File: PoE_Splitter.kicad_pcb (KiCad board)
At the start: 2 copper layers, 104 x 62 mm, 120 parts, among them J1 R-RJ45R10P-B000, J2 R-RJ45R10P-B000, J3 AMASS_XT30PW-M, J4 AMASS_XT30PW-M, J5 AMASS_XT30PW-M, Q1 BSS127S, U1 VCF4812EBO-120WR3-N, U2 TPS2372, U3 MPQ8875A, U4 PD70224, U5 USBLC6-2P6

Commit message: minor cap footprint and value changes
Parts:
- C34, C40: value 2.2uF -> 1uF
- C35, C53: value 2.2uF -> 100nF
- C48, C49: footprint Capacitor_SMD:C_1808_4520Metric -> Capacitor_SMD:C_1812_4532Metric
- moved C48 0.55 mm to (187.8, 104.7)
- moved C49 0.55 mm to (176.1, 104.7)
- moved C28 0.10 mm to (164.2, 107.5)
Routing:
- net AUX_OUT+: vias 5 -> 10

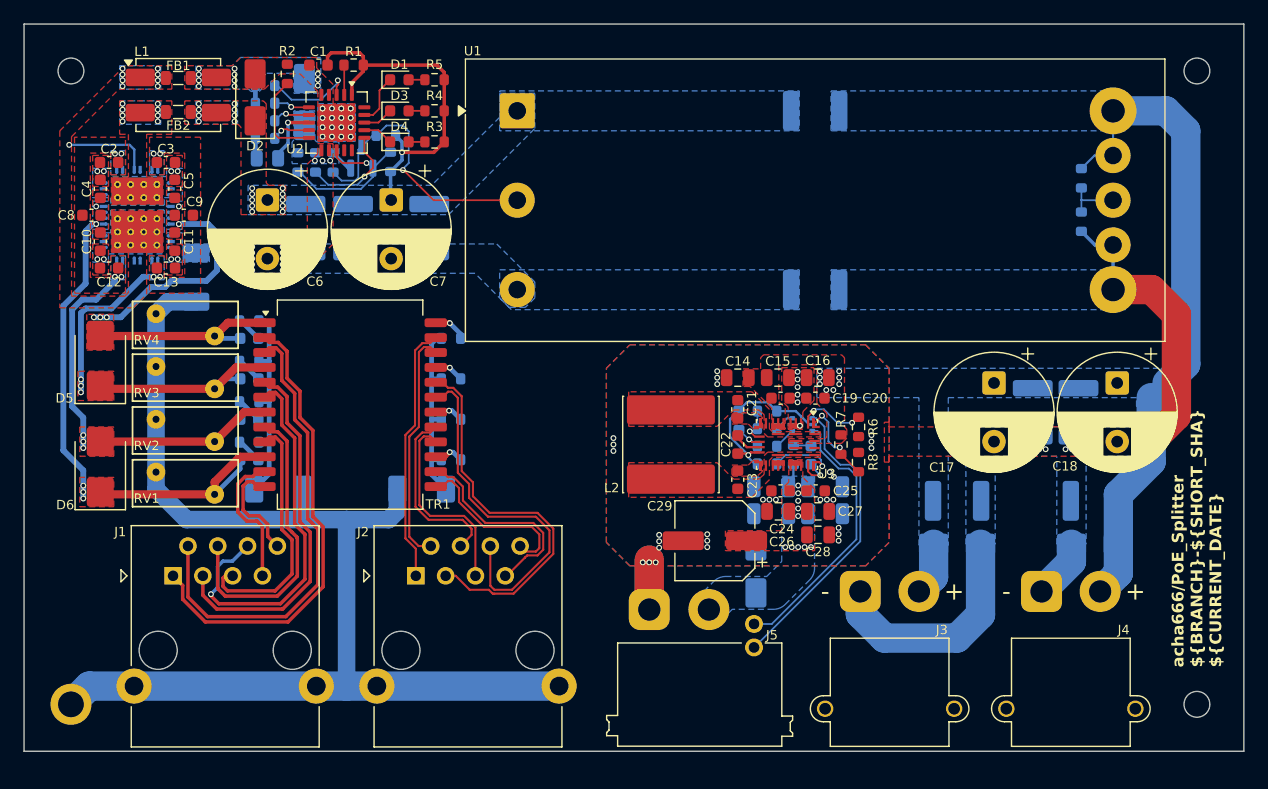
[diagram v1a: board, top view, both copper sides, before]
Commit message: fix: pd70224 input connection
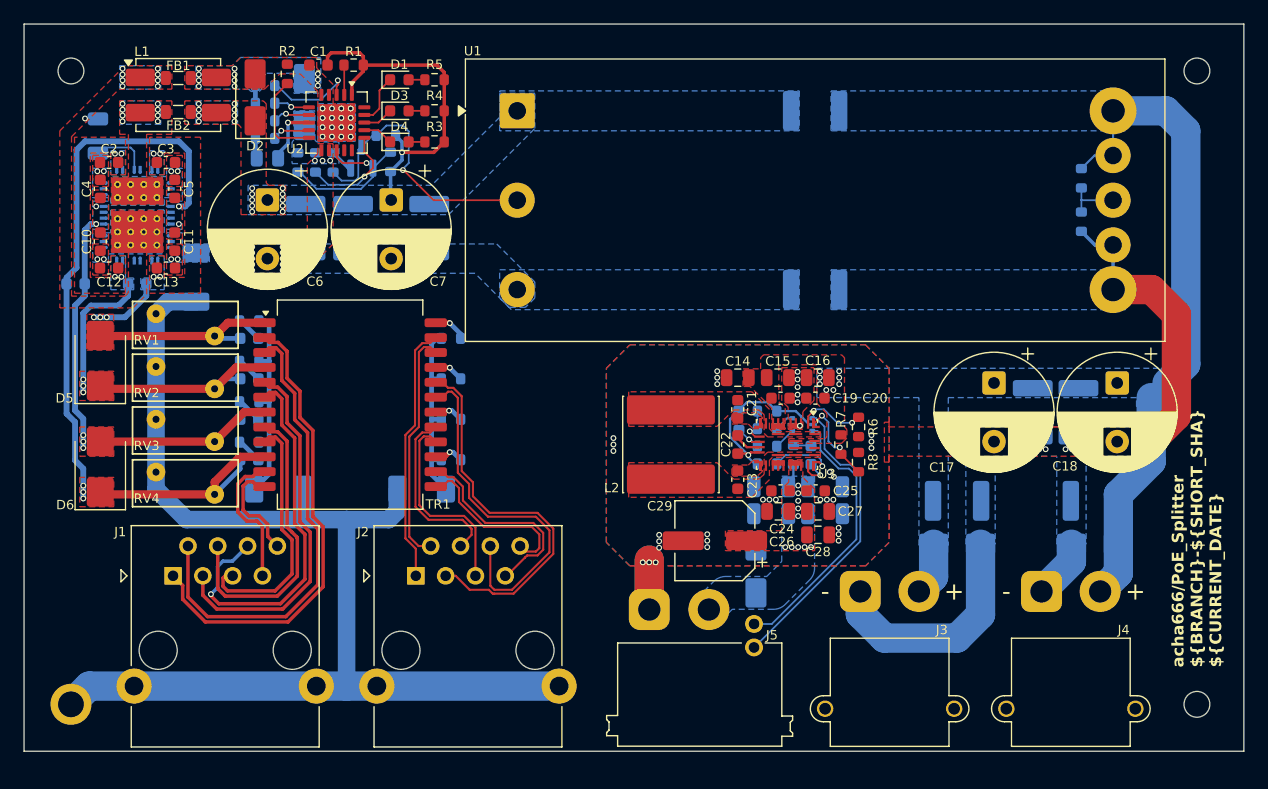
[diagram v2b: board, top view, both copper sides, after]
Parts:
- added R35: 0Ω, Resistor_SMD:R_1206_3216Metric, B.Cu at (102.8, 73.5)
- C8, C9: moved to B.Cu
- moved C9 7.07 mm to (106.2, 86.2), turned to 0 degrees
- moved C8 6.00 mm to (100.9, 86.2), turned to 180 degrees
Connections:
- C10 pad 1: /RJ45 Ports/PS+ -> /RJ45 Ports/PS-
- C11 pad 1: /RJ45 Ports/PD- -> /RJ45 Ports/PS+
- C12 pad 1: /RJ45 Ports/PS- -> /RJ45 Ports/PD+
- C13 pad 1: /RJ45 Ports/PD+ -> /RJ45 Ports/PD-
- C2 pad 2: /RJ45 Ports/PS- -> /RJ45 Ports/PD+
- C3 pad 2: /RJ45 Ports/PD+ -> /RJ45 Ports/PD-
- C4 pad 2: /RJ45 Ports/PS+ -> /RJ45 Ports/PS-
- C5 pad 2: /RJ45 Ports/PD- -> /RJ45 Ports/PS+
- U4 pad 11: /RJ45 Ports/PD+ -> /RJ45 Ports/PD-
- U4 pad 12: /RJ45 Ports/PD+ -> /RJ45 Ports/PD-
- U4 pad 15: /RJ45 Ports/PS- -> /RJ45 Ports/PD+
- U4 pad 16: /RJ45 Ports/PS- -> /RJ45 Ports/PD+
- U4 pad 20: /RJ45 Ports/PS+ -> /RJ45 Ports/PS-
- U4 pad 21: /RJ45 Ports/PS+ -> /RJ45 Ports/PS-
- U4 pad 22: /RJ45 Ports/PS+ -> /RJ45 Ports/PS-
- U4 pad 23: /RJ45 Ports/PS+ -> /RJ45 Ports/PS-
- U4 pad 27: /RJ45 Ports/PS- -> /RJ45 Ports/PD+
- U4 pad 28: /RJ45 Ports/PS- -> /RJ45 Ports/PD+
- U4 pad 29: VRECT- -> Net-(U4-WA_EN)
- U4 pad 31: /RJ45 Ports/PD+ -> /RJ45 Ports/PD-
- U4 pad 32: /RJ45 Ports/PD+ -> /RJ45 Ports/PD-
- U4 pad 4: /RJ45 Ports/PD- -> /RJ45 Ports/PS+
- U4 pad 5: /RJ45 Ports/PD- -> /RJ45 Ports/PS+
- U4 pad 6: /RJ45 Ports/PD- -> /RJ45 Ports/PS+
- U4 pad 7: /RJ45 Ports/PD- -> /RJ45 Ports/PS+
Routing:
- net /RJ45 Ports/PS+: track 45.0 -> 65.9 mm
- net /RJ45 Ports/PD-: track 35.3 -> 22.7 mm, vias 5 -> 7
- net VRECT-: track 7.39 -> 1.12 mm
- net Net-(U4-WA_EN): track 0.00 -> 4.37 mm
- net /RJ45 Ports/PS-: track 35.2 -> 38.4 mm, vias 7 -> 5
- net /RJ45 Ports/PD+: track 31.3 -> 29.2 mm

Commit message: move connectors update 3d models
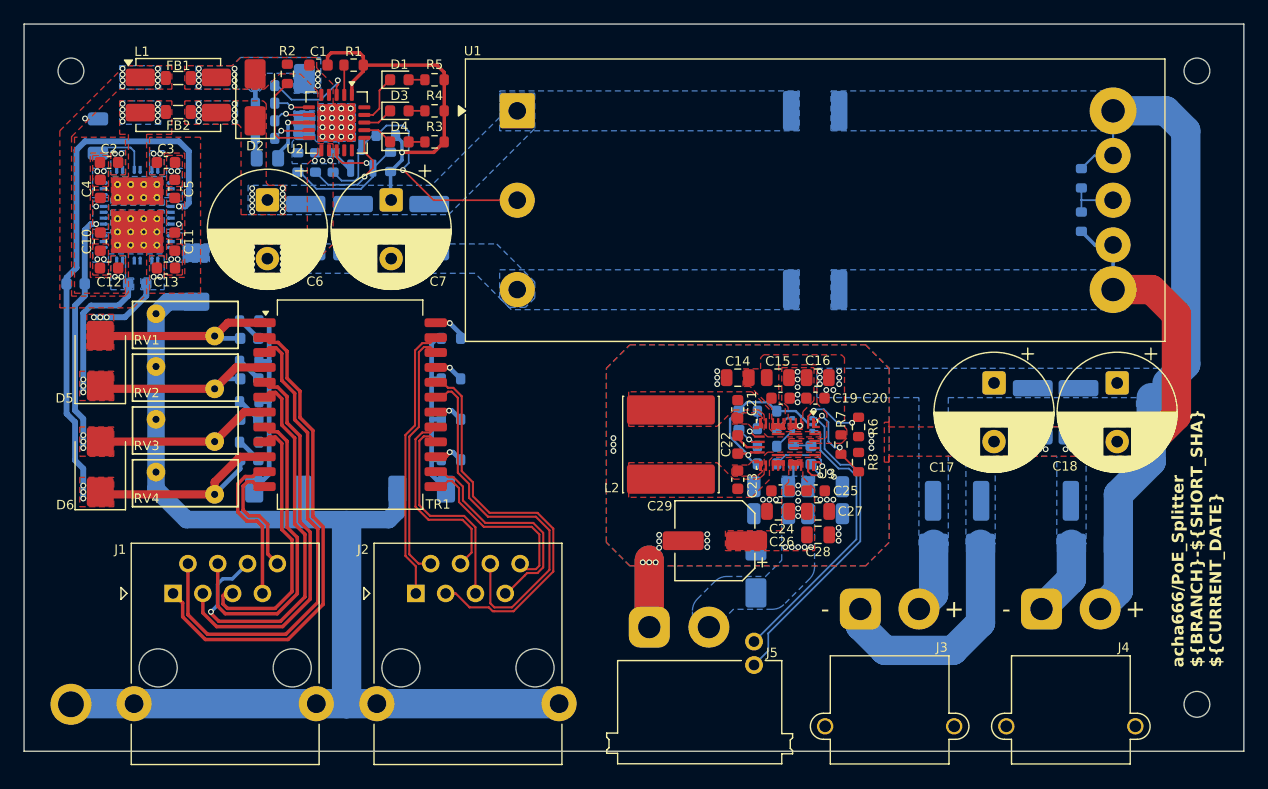
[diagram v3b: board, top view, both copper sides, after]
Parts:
- moved J1 1.50 mm to (109.2, 112.5)
- moved J2 1.50 mm to (129.9, 112.5)
- moved J3 1.50 mm to (167.8, 113.9)
- moved J4 1.50 mm to (183.2, 113.9)
- moved J5 1.50 mm to (154.3, 117.0)
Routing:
- net VOUT-: track 60.6 -> 65.4 mm
- net VOUT+: track 58.9 -> 61.9 mm
- net /SDA: track 25.7 -> 27.2 mm
- net /RJ45 Ports/TD1-: track 40.1 -> 41.6 mm
- net /RJ45 Ports/TD2+: track 31.3 -> 32.8 mm
- net /RJ45 Ports/MX1+: track 22.1 -> 23.6 mm
- net /RJ45 Ports/TD4-: track 8.40 -> 9.90 mm
- net /RJ45 Ports/TD4+: track 11.3 -> 12.8 mm
- net /RJ45 Ports/TD2-: track 33.3 -> 34.8 mm
- net /RJ45 Ports/TD1+: track 40.1 -> 41.6 mm
- net /RJ45 Ports/MX4-: track 14.2 -> 15.7 mm
- net /RJ45 Ports/MX3-: track 16.9 -> 18.4 mm
- net /RJ45 Ports/MX3+: track 15.3 -> 16.8 mm
- net /RJ45 Ports/MX2+: track 32.4 -> 33.9 mm
- net /RJ45 Ports/MX1-: track 20.1 -> 21.6 mm
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
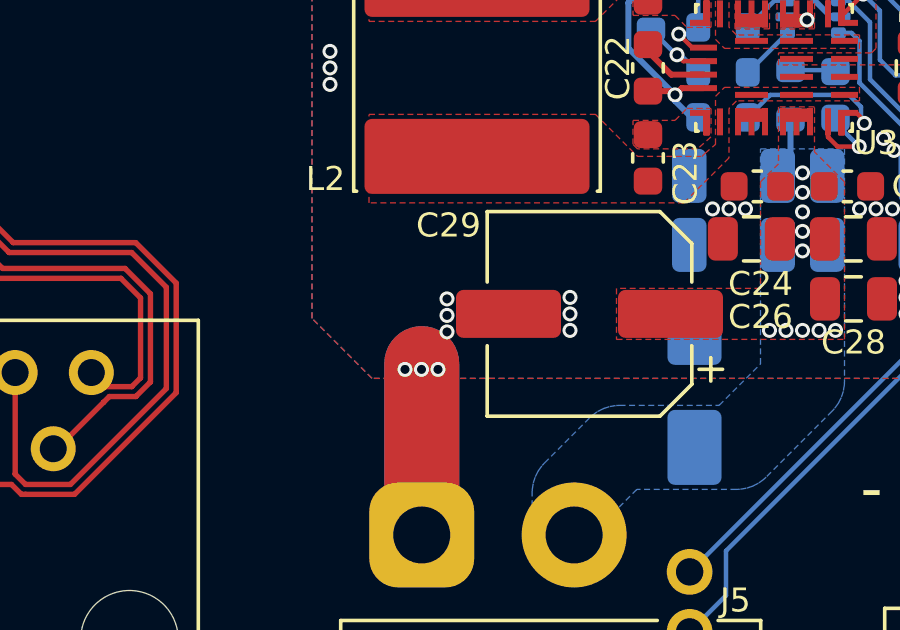
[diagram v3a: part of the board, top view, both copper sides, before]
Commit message: change C29 footprint XT30 3d model position
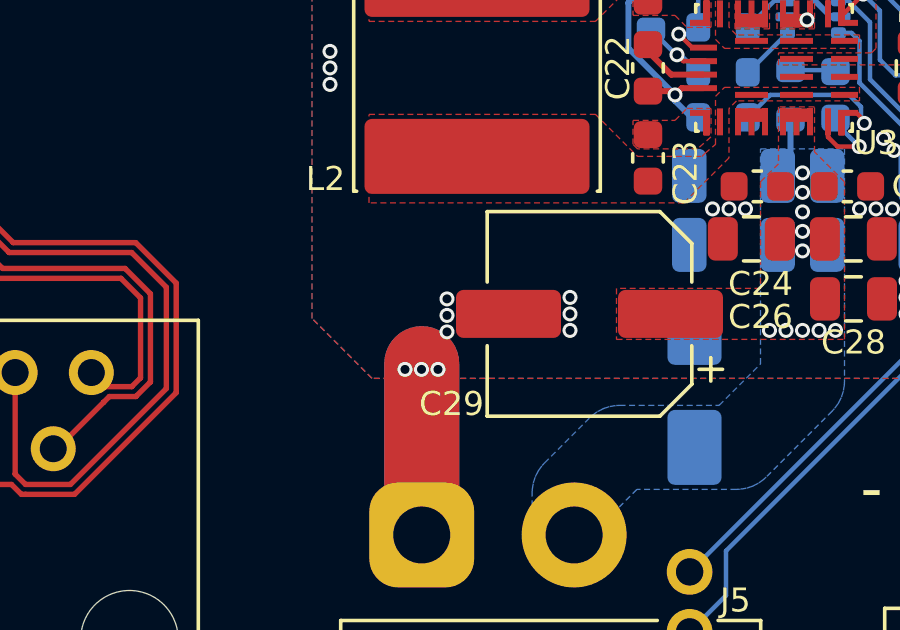
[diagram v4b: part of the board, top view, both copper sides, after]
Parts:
- C29: footprint Capacitor_SMD:CP_Elec_6.3x5.7 -> Capacitor_SMD:CP_Elec_6.3x7.7
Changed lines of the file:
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@@
 		(model "${KIPRJMOD}/PoE_Splitter.3dshapes/AMASS_XT30PW(2+2)-M_Horizontal.wrl"
 			(offset
-				(xyz -0.172 -3.85 0)
+				(xyz -0.144 -3.85 0)
 			)
 			(scale
@@
 		)
 	)
-	(footprint "Capacitor_SMD:CP_Elec_6.3x5.7"
+	(footprint "Capacitor_SMD:CP_Elec_6.3x7.7"
 		(layer "F.Cu")
 		(at 155.4 108.05 180)
-		(descr "SMD capacitor, aluminum electrolytic, United Chemi-Con, 6.3x5.7mm")
+		(descr "SMD capacitor, aluminum electrolytic, Nichicon, 6.3x7.7mm")
 		(tags "capacitor electrolytic")
 		(property "Reference" "C29"
-			(at 4.7 2.95 0)
+			(at 4.6 -3 180)
 			(layer "F.SilkS")
 			(effects
@@
 			(at 0 4.35 180)
 			(layer "F.Fab")
-			(hide yes)
 			(effects
 				(font
@@
 		)
 		(embedded_fonts no)
-		(model "${KICAD10_3DMODEL_DIR}/Capacitor_SMD.3dshapes/CP_Elec_6.3x5.7.step"
+		(model "${KICAD10_3DMODEL_DIR}/Capacitor_SMD.3dshapes/CP_Elec_6.3x7.7.step"
 			(offset
 				(xyz 0 0 0)

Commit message: value text visibility on Fab layer
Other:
- board text removed: "3.0SMBJ58CA"
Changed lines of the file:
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@@
 			(at 0 4.35 180)
 			(layer "F.Fab")
+			(hide yes)
 			(effects
 				(font
@@
 			(at 0 -2.65 0)
 			(layer "B.Fab")
+			(hide yes)
 			(effects
 				(font
@@
 			(at 0 -1.83 90)
 			(layer "B.Fab")
+			(hide yes)
 			(effects
 				(font
@@
 			(at 0 -2.65 180)
 			(layer "B.Fab")
+			(hide yes)
 			(effects
 				(font
@@
 		)
 	)
-	(gr_text "3.0SMBJ58CA"
-		(at 77.627649 90.673718 90)
-		(layer "B.Fab")
-		(effects
-			(font
-				(size 1 1)
-				(thickness 0.15)
-			)
-			(justify mirror)
-		)
-	)
-	(gr_text "3.0SMBJ58CA"
-		(at 77.6292 81.6796 90)
-		(layer "B.Fab")
-		(effects
-			(font
-				(size 1 1)
-				(thickness 0.15)
-			)
-			(justify mirror)
-		)
-	)

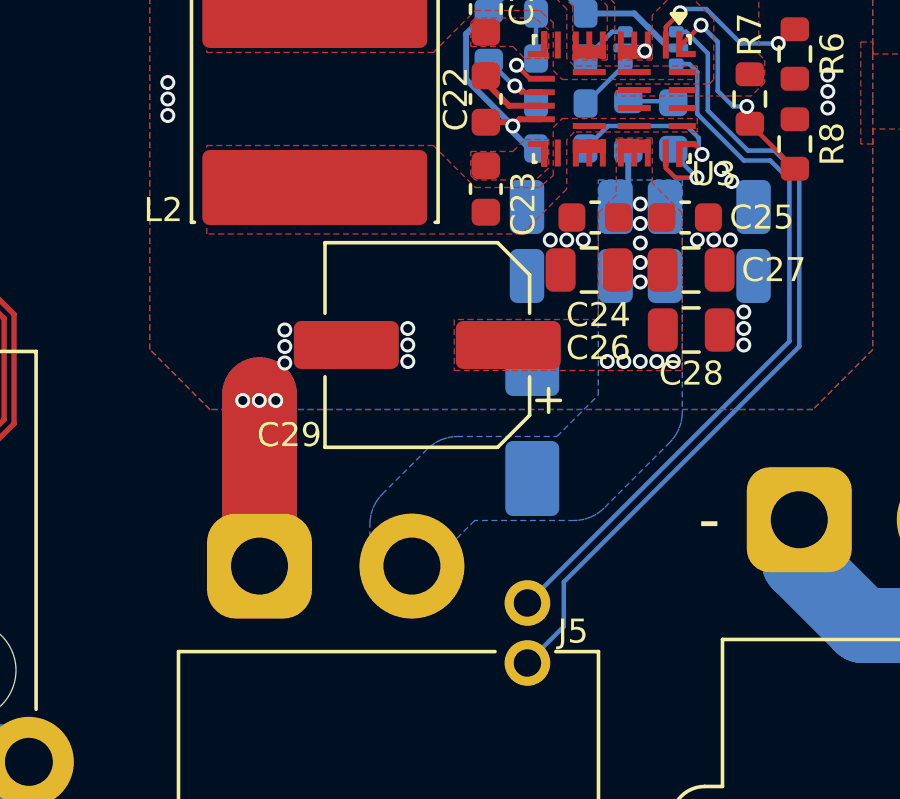
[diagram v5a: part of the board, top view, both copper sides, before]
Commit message: J5 footprint polarity
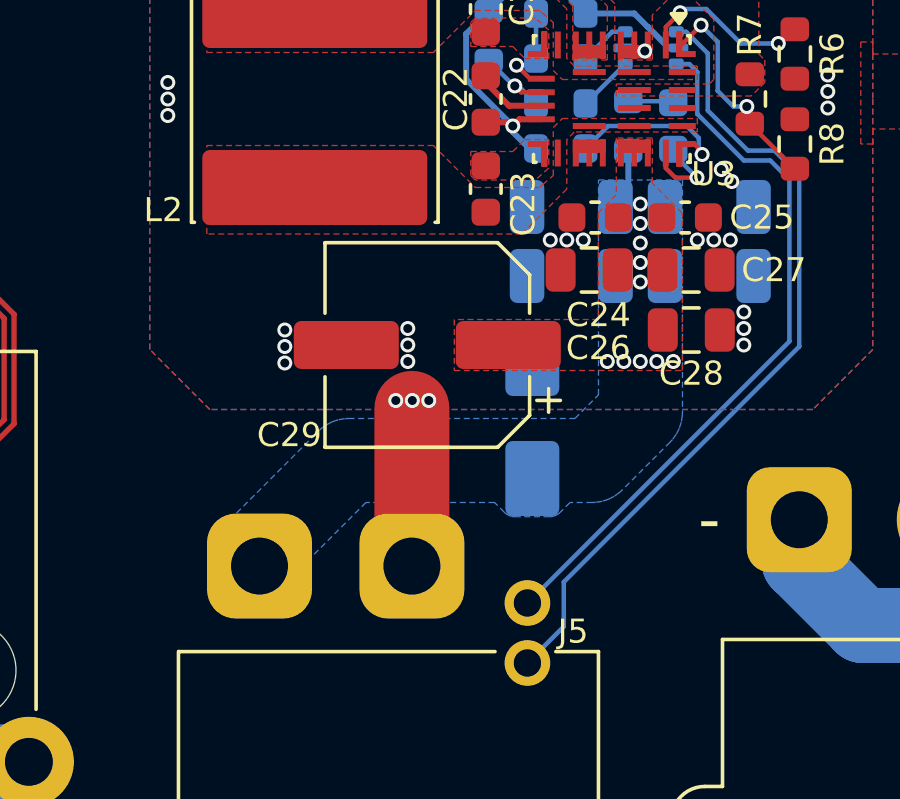
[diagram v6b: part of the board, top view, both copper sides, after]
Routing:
- net VOUT-: track 65.4 -> 59.3 mm
